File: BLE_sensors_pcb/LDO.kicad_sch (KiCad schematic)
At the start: 3 parts, among them U6 TLV70018_SOT23-5

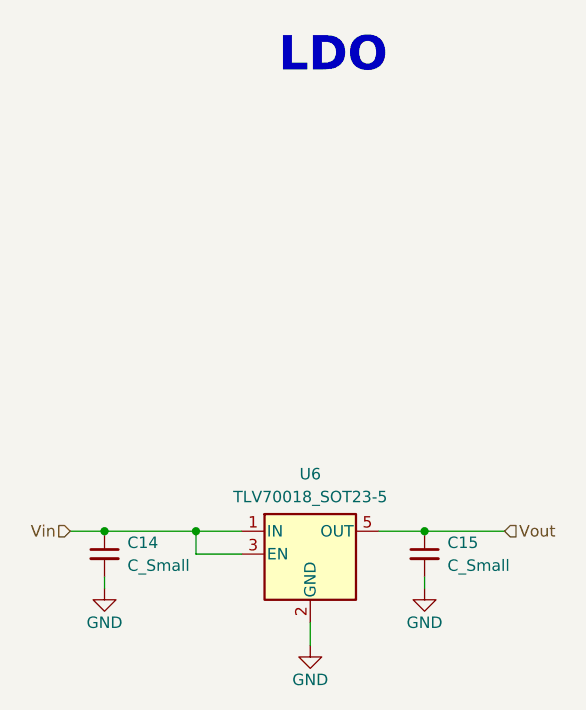
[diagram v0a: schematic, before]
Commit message: Added the usb to serial bridge
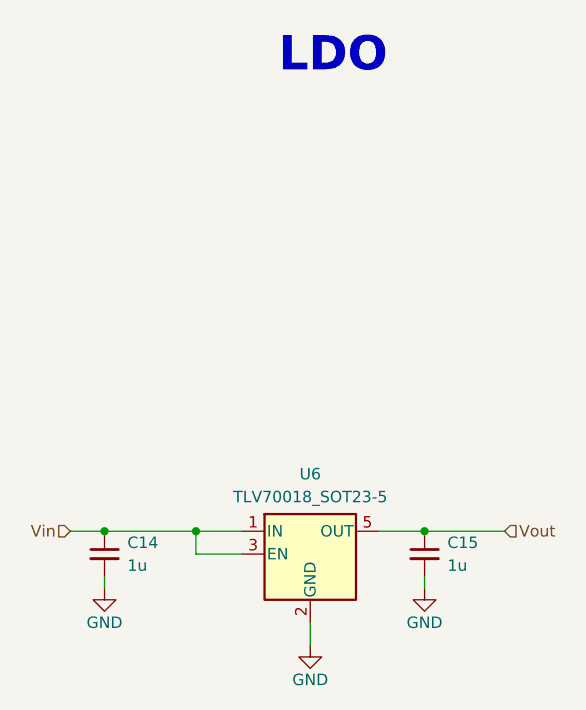
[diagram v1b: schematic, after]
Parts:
- C14, C15: value C_Small -> 1u
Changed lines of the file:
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@@
 			)
 		)
-		(property "Value" "C_Small"
+		(property "Value" "1u"
 			(at 151.13 105.4162 0)
 			(effects
@@
 			)
 		)
-		(property "Value" "C_Small"
+		(property "Value" "1u"
 			(at 115.57 105.4162 0)
 			(effects

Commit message: Footprints and some pcb placement
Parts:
- C14, C15: footprint (none) -> Capacitor_SMD:C_0603_1608Metric
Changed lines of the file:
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@@
 			)
 		)
-		(property "Footprint" ""
+		(property "Footprint" "Capacitor_SMD:C_0603_1608Metric"
 			(at 148.59 104.14 0)
 			(effects
@@
 			)
 		)
-		(property "Footprint" ""
+		(property "Footprint" "Capacitor_SMD:C_0603_1608Metric"
 			(at 113.03 104.14 0)
 			(effects
